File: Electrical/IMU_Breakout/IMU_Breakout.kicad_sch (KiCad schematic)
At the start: 9 parts, among them J1 Conn_01x04_Pin, J2 Conn_01x04_Pin, U1 BMI323

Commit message: Finalize IMU Breakout board
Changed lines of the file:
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@@
   (symbol (lib_id "Connector:Conn_01x04_Pin") (at 170.815 81.28 0) (unit 1)
     (in_bom yes) (on_board yes) (dnp no)
-    (property "Reference" "J1" (at 171.45 73.66 0)
+    (property "Reference" "J1" (at 171.45 88.265 0)
       (effects (font (size 1.27 1.27)))
     )
-    (property "Value" "Conn_01x04_Pin" (at 172.085 93.98 0)
+    (property "Value" "Conn_01x04_Pin" (at 171.45 90.17 0)
       (effects (font (size 1.27 1.27)))
     )

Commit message: Update header blocks
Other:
- title: Test sheet -> BMI323 Breakout Board
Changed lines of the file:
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@@
   (paper "B")
   (title_block
-    (title "Test sheet")
+    (title "BMI323 Breakout Board")
+    (date "2024-03-10")
     (rev "0.1")
     (company "satomm@stanford.edu")

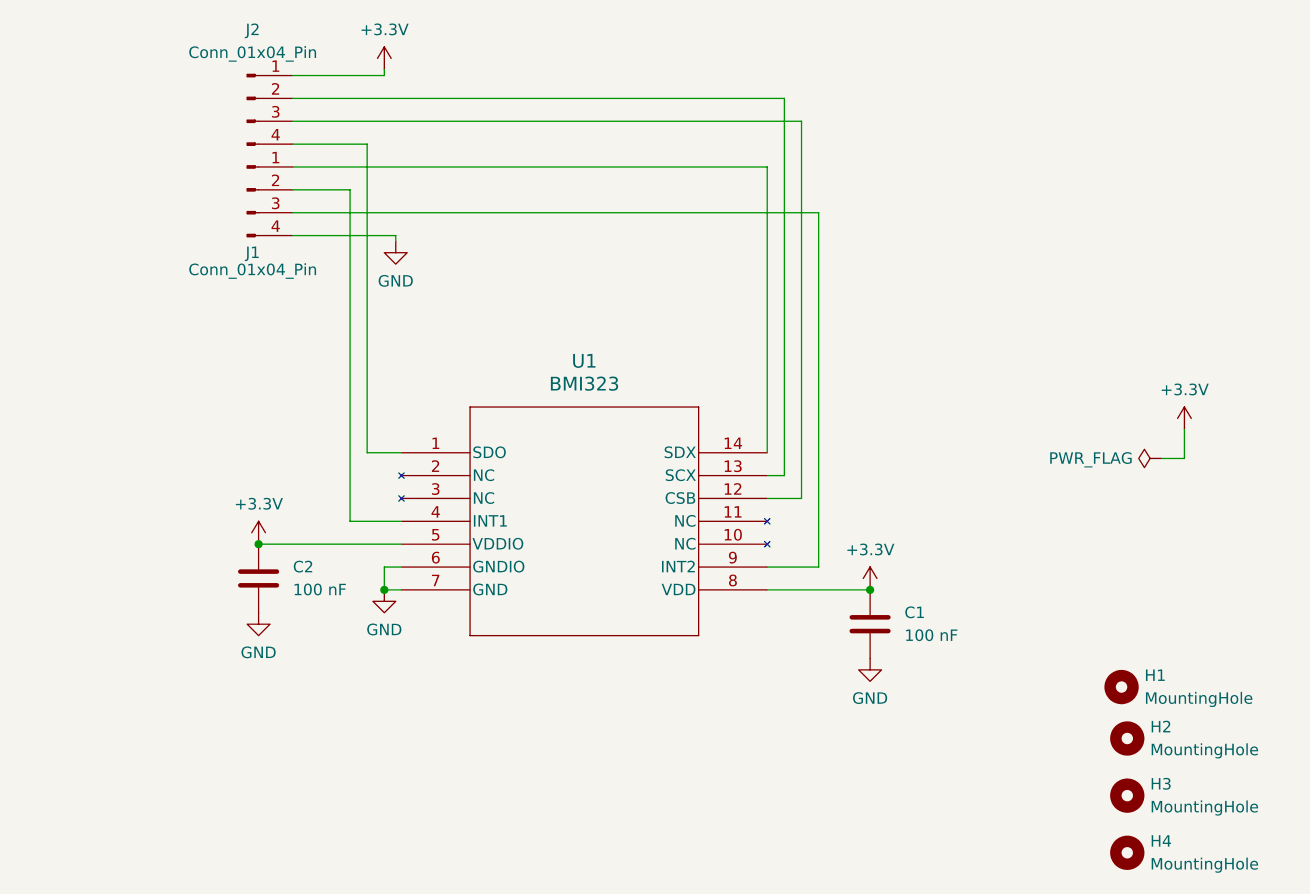
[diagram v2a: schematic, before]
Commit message: Update the connection for IMU breakout board
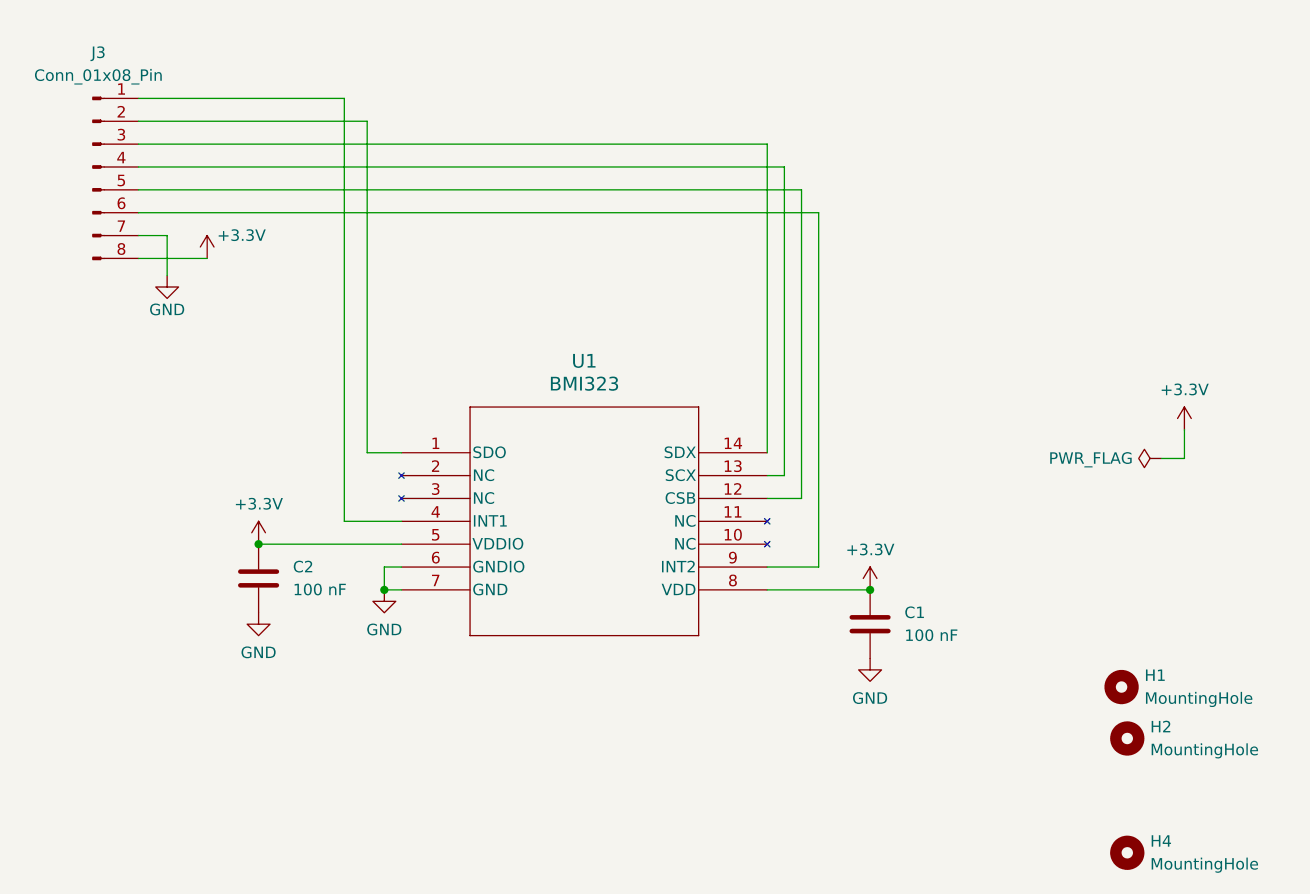
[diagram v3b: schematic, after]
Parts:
- removed H3: MountingHole, MountingHole:MountingHole_3.2mm_M3, symbol Mechanical:MountingHole
- removed J1, J2: Conn_01x04_Pin, Connector_PinSocket_2.54mm:PinSocket_1x04_P2.54mm_Vertical, symbol Connector:Conn_01x04_Pin
- added J3: Conn_01x08_Pin, Connector_Molex:Molex_PicoBlade_53048-0810_1x08_P1.25mm_Horizontal, symbol Connector:Conn_01x08_Pin
- H1, H2, H4: now left out of the parts list
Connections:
- net +3.3V: now also J3.8 (Pin_8)
- net GND: now also J3.7 (Pin_7)
- net at U1.1 (SDO): now also J3.2 (Pin_2)
- net at U1.12 (CSB): now also J3.5 (Pin_5)
- net at U1.13 (SCX): now also J3.4 (Pin_4)
- net at U1.14 (SDX): now also J3.3 (Pin_3)
- net at U1.4 (INT1): now also J3.1 (Pin_1)
- net at U1.9 (INT2): now also J3.6 (Pin_6)
